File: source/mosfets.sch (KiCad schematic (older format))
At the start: 65 parts, among them Q1 NCEP60T20, Q2 NCEP60T20, Q3 NCEP60T20, Q4 NCEP60T20, Q5 NCEP60T20

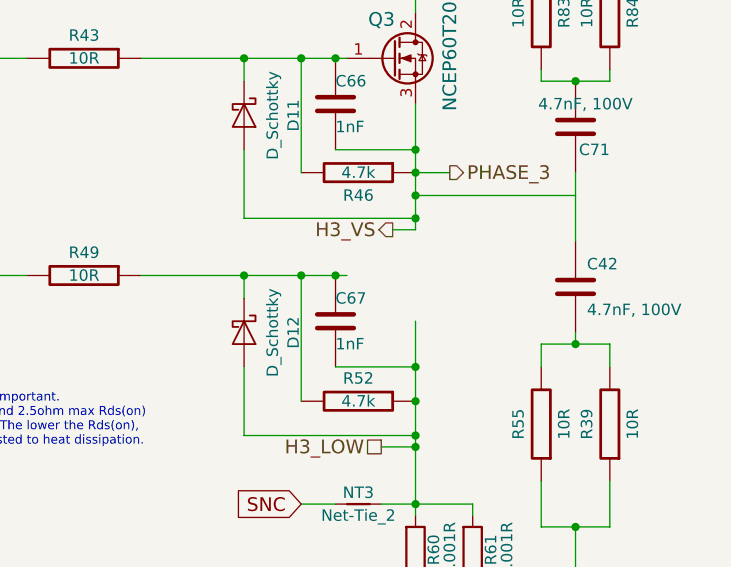
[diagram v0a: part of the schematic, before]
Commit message: Put back Q6 which was accidentally deleted
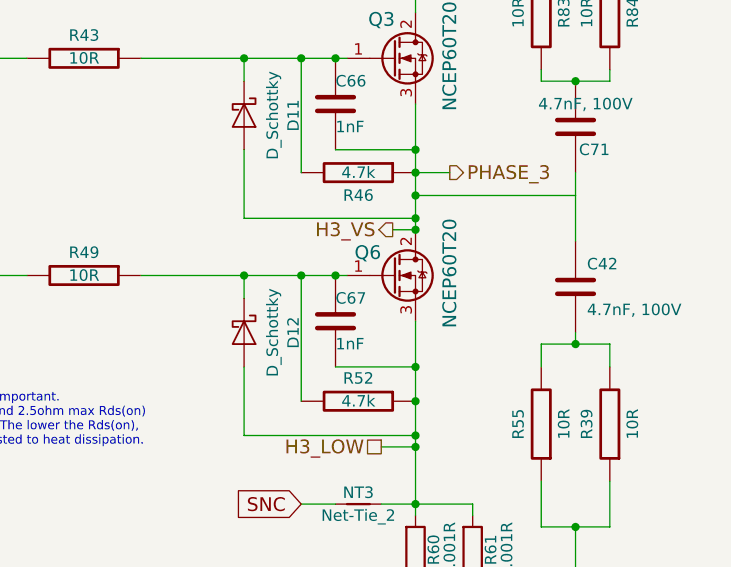
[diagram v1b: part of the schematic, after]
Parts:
- added Q6: NCEP60T20, shapes3D:TO-220-3_Horizontal_TabUp_no_hole, symbol Device:Q_NMOS_GDS
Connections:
- net H3_LOW: now also Q6.3 (S)
- net H3_VS: now also Q6.2 (D)
- net at C67.1, D12.1 (K), R49.1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: now also Q6.1 (G)
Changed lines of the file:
@@
 Sheet 5 8
 Title "Cheap FOCer 2"
-Date "2020-04-08"
-Rev "0.9"
+Date "2021-06-25"
+Rev "1.0"
 Comp "Shaman Systems"
 Comment1 "Root"
@@
 Wire Wire Line
 	8650 4200 9100 4200
+$Comp
+L Device:Q_NMOS_GDS Q6
+U 1 1 60D6EF49
+P 9750 4200
+F 0 "Q6" H 9700 4300 60  0000 R CNN
+F 1 "NCEP60T20" V 10000 4450 60  0000 R CNN
+F 2 "shapes3D:TO-220-3_Horizontal_TabUp_no_hole" H 9750 4200 60  0001 C CNN
+F 3 "" H 9750 4200 60  0001 C CNN
+	1    9750 4200
+	1    0    0    -1
+$EndComp
+Connection ~ 9850 4000
 $EndSCHEMATC

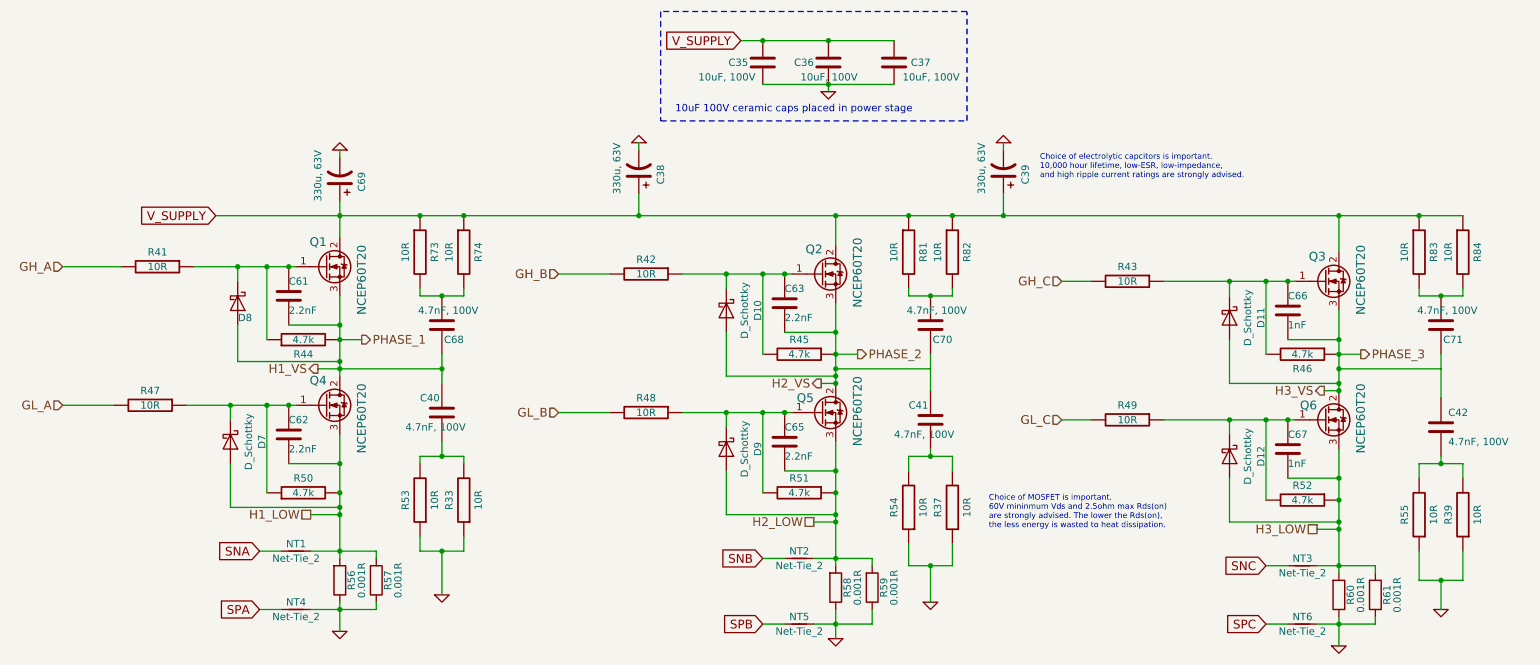
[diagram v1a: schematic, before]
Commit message: Revert "Remove transistors"
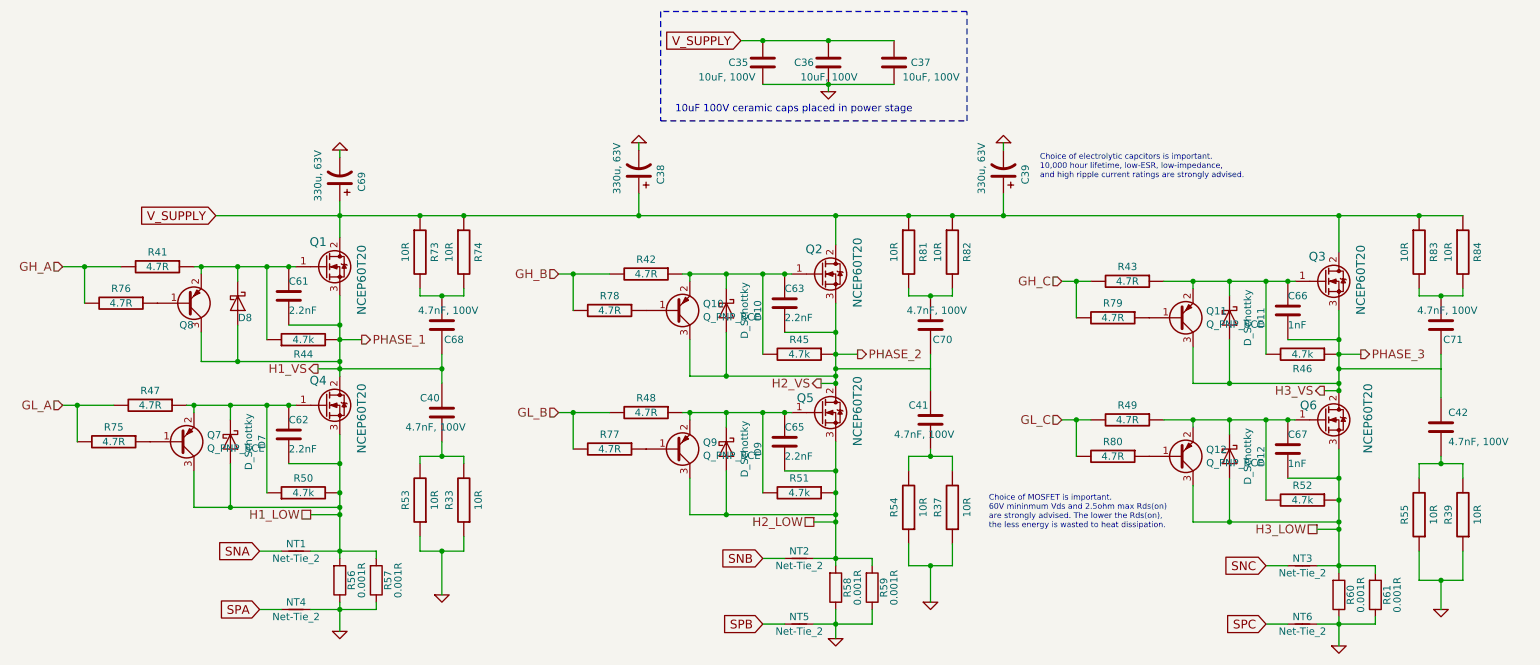
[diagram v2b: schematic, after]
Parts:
- added Q10, Q11, Q12, Q7, Q8, Q9: Q_PNP_BCE, Package_TO_SOT_SMD:SOT-23, symbol Device:Q_PNP_BEC
- added R75, R76, R77, R78, R79, R80: 4.7R, Resistor_SMD:R_0603_1608Metric, symbol BLDC_4-rescue:R-RESCUE-BLDC_4
- R41, R42, R43, R47, R48, R49: value 10R -> 4.7R
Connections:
- net GH_A: now also R76.2
- net GH_B: now also R78.2
- net GH_C: now also R79.2
- net GL_A: now also R75.2
- net GL_B: now also R77.2
- net GL_C: now also R80.2
- net H1_LOW: now also Q7.3 (C)
- net H1_VS: now also Q8.3 (C)
- net H2_LOW: now also Q9.3 (C)
- net H2_VS: now also Q10.3 (C)
- net H3_LOW: now also Q12.3 (C)
- net H3_VS: now also Q11.3 (C)
- net at C61.1, D8.1 (K), Q1.1 (G)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: now also Q8.2 (E)
- net at C62.1, D7.1 (K), Q4.1 (G)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: now also Q7.2 (E)
- net at C65.1, D9.1 (K), Q5.1 (G)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: now also Q9.2 (E)
- net at C63.1, D10.1 (K), Q2.1 (G)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: now also Q10.2 (E)
- net at C66.1, D11.1 (K), Q3.1 (G)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: now also Q11.2 (E)
- net at C67.1, D12.1 (K), Q6.1 (G)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: now also Q12.2 (E)
- new net: Q8.1 (B), R76.1
- new net: Q7.1 (B), R75.1
- new net: Q10.1 (B), R78.1
- new net: Q11.1 (B), R79.1
- new net: Q12.1 (B), R80.1
- new net: Q9.1 (B), R77.1

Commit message: removed transistors from the gate of the mosfets and fixed the config file for compiling the firmware
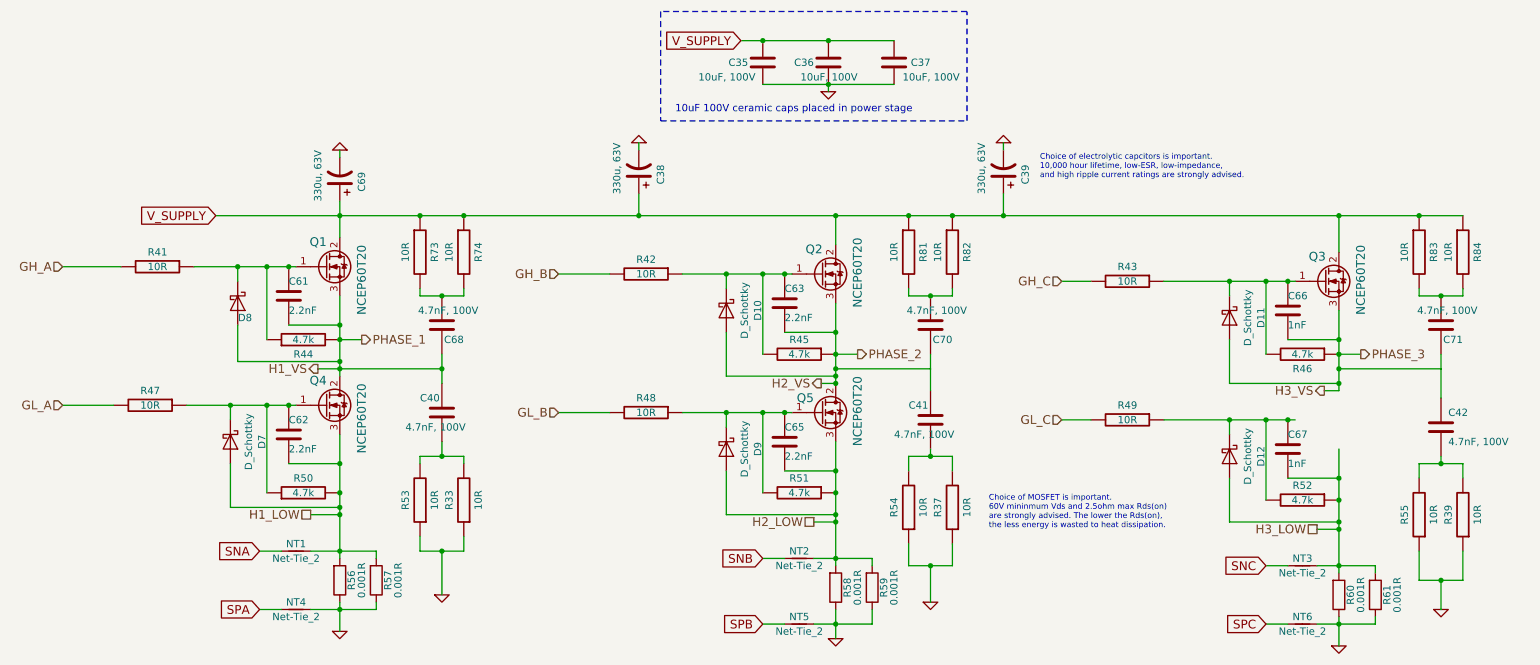
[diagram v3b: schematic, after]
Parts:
- removed Q10, Q11, Q12, Q7, Q8, Q9: Q_PNP_BCE, Package_TO_SOT_SMD:SOT-23, symbol Device:Q_PNP_BEC
- removed Q6: NCEP60T20, shapes3D:TO-220-3_Horizontal_TabUp_no_hole, symbol Device:Q_NMOS_GDS
- removed R75, R76, R77, R78, R79, R80: 4.7R, Resistor_SMD:R_0603_1608Metric, symbol BLDC_4-rescue:R-RESCUE-BLDC_4
- R41, R42, R43, R47, R48, R49: value 4.7R -> 10R
